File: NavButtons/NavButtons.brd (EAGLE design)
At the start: 35.6 x 29.8 mm, 11 parts

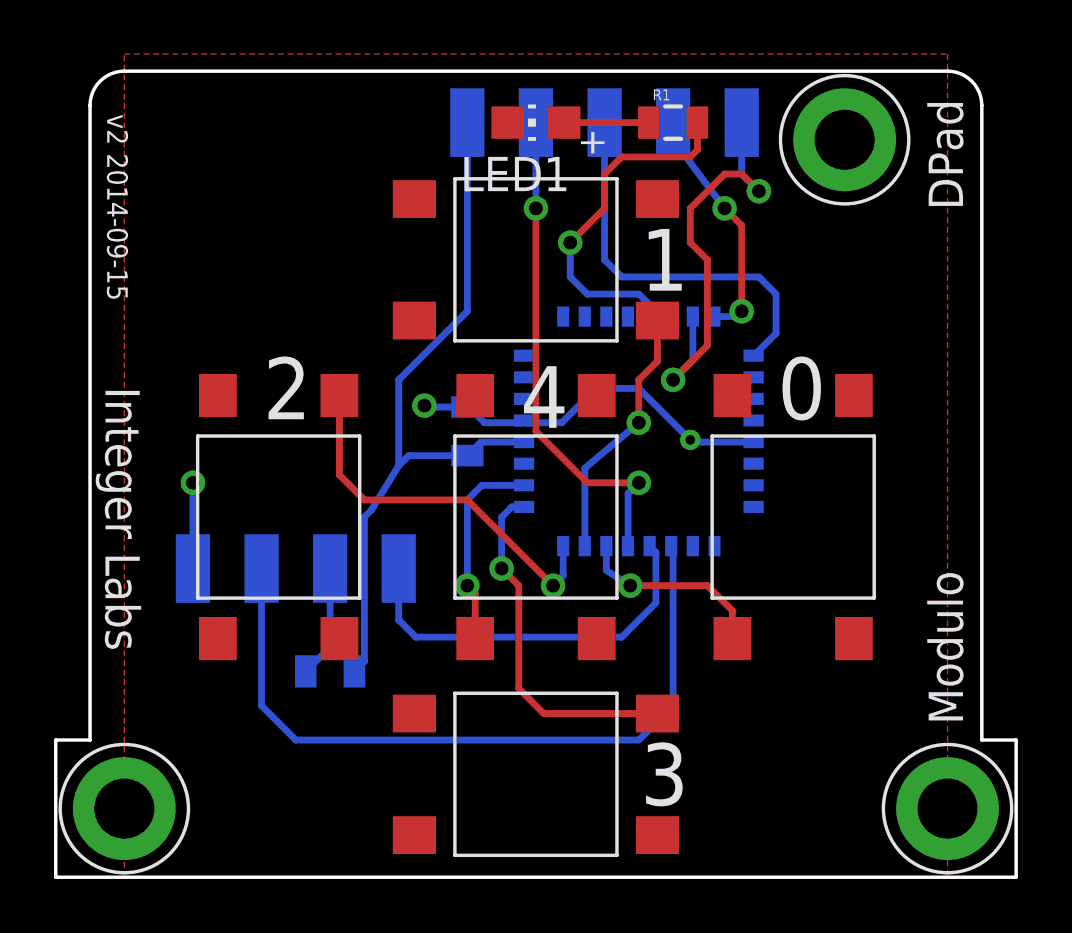
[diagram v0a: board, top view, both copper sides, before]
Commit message: Changed NavButtons back to using attiny441
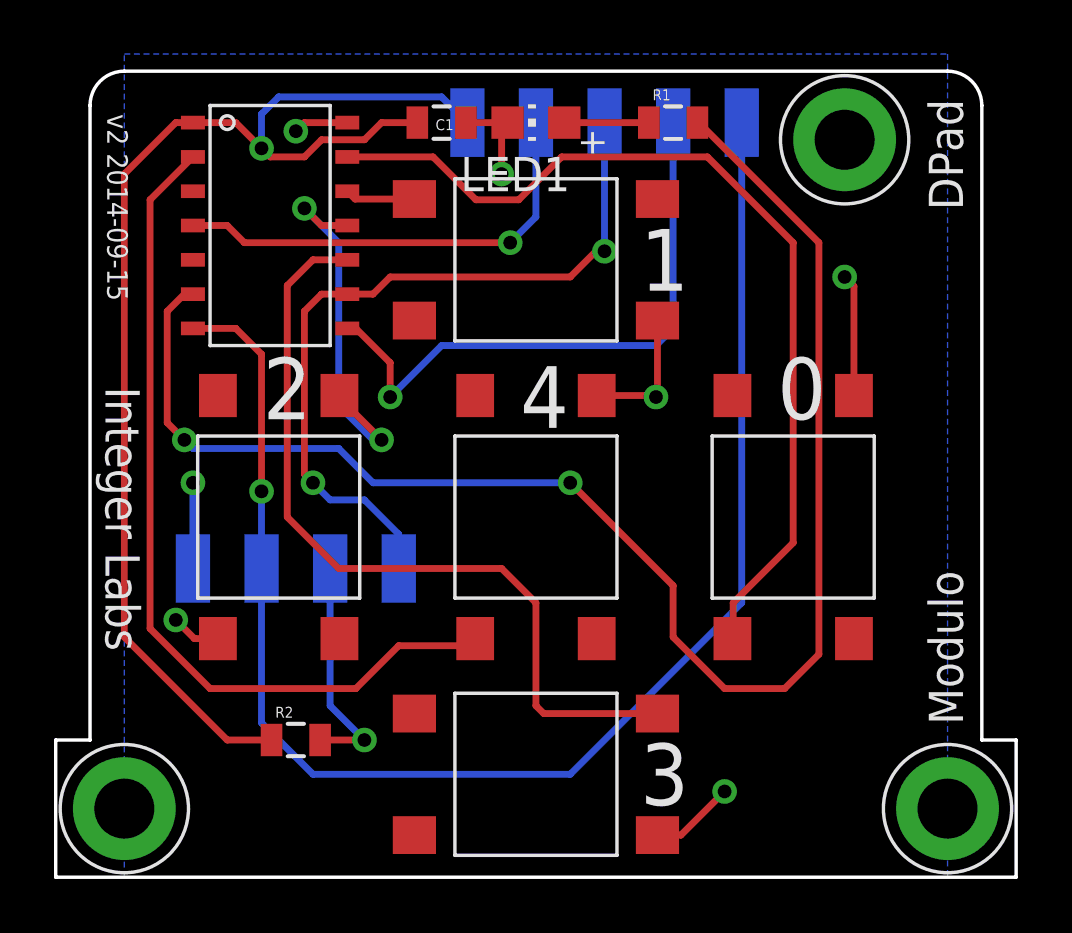
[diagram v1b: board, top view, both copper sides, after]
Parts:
- removed U$5: ATTINY48/88-TQFP, IntegerLabs:TQFP-32
- added U$1: TINY841, IntegerLabs:SOIC14
- moved C1 11.5 mm to (14.3, 27.9), flipped to the top, turned to 180 degrees
- moved R2 2.84 mm to (8.89, 5.08), flipped to the top
- turned B1 to 0 degrees
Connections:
- removed net AVCC: U$5.18
- removed net MOSI: U$2.PROG4, U$5.15
- removed net SCK: U$2.PROG2, U$5.17
- removed net SCL: U$2.BUS3, U$5.28
- removed net SDA: U$2.BUS1, U$5.27
- removed net THERM: U$5.25
- new net SCL/SCK: U$1.9, U$2.BUS3, U$2.PROG2
- new net SDA/MOSI: U$1.7, U$2.BUS1, U$2.PROG4
- net BUTTON0: now also U$1.13; no longer U$5.30
- net BUTTON1: now also U$1.12; no longer U$5.31
- net BUTTON2: now also U$1.11; no longer U$5.32
- net BUTTON3: now also U$1.10; no longer U$5.1
- net BUTTON4: now also U$1.2; no longer U$5.2
- net GND: now also U$1.14; no longer U$5.21, U$5.5
- net LED: now also U$1.6; no longer U$5.13
- net MISO: now also U$1.8; no longer U$5.16
- net RESET: now also U$1.4; no longer U$5.29
- net VCC: now also U$1.1; no longer U$5.4
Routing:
- net SDA/MOSI: track 0.00 -> 55.6 mm, vias 0 -> 1
- net LED: track 13.0 -> 56.8 mm, vias 1 -> 2
- net SCL/SCK: track 0.00 -> 28.5 mm, vias 0 -> 2
- net BUTTON0: track 7.15 -> 34.7 mm, vias 1 -> 0
- net SDA: track 27.3 -> 0.00 mm
- net BUTTON4: track 7.58 -> 31.8 mm, vias 1 -> 0
- net VCC: track 26.9 -> 46.4 mm, vias 0 -> 1
- net BUTTON3: track 13.1 -> 30.1 mm, vias 1 -> 0
- net MOSI: track 15.9 -> 0.00 mm, vias 2 -> 0
- net SCK: track 14.6 -> 0.00 mm
- net SCL: track 14.4 -> 0.00 mm
- net MISO: track 8.97 -> 22.5 mm, vias 2 -> 1
- net BUTTON1: track 9.57 -> 2.61 mm, vias 1 -> 0
- net GND: track 17.4 -> 23.4 mm, vias 3 -> 7
- net N$2: track 4.18 -> 8.52 mm, vias 0 -> 1
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- added copper zone on layer 16, net GND
- removed copper zone on layer 1, net GND
